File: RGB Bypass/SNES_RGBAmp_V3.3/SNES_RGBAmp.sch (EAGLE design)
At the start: 25 parts

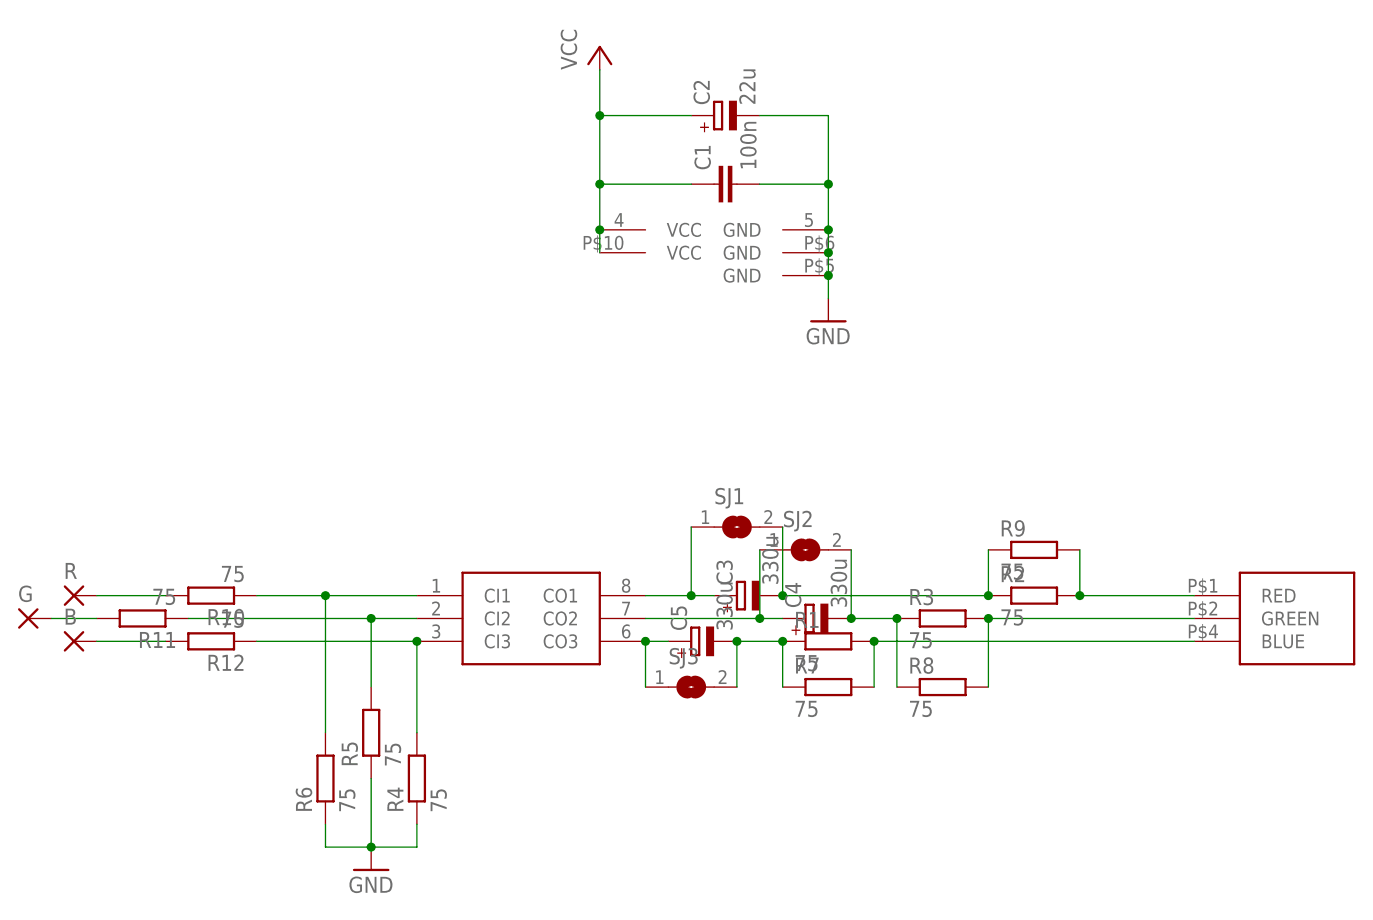
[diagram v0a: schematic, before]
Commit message: RGB Bypass Version Update: - adjustment of wires - mirrored positioning of R, G and B pad - exact values for resistors - add a version with CSYNC-buffering (for 1Chip03 boards and later) - more detailed notes in README
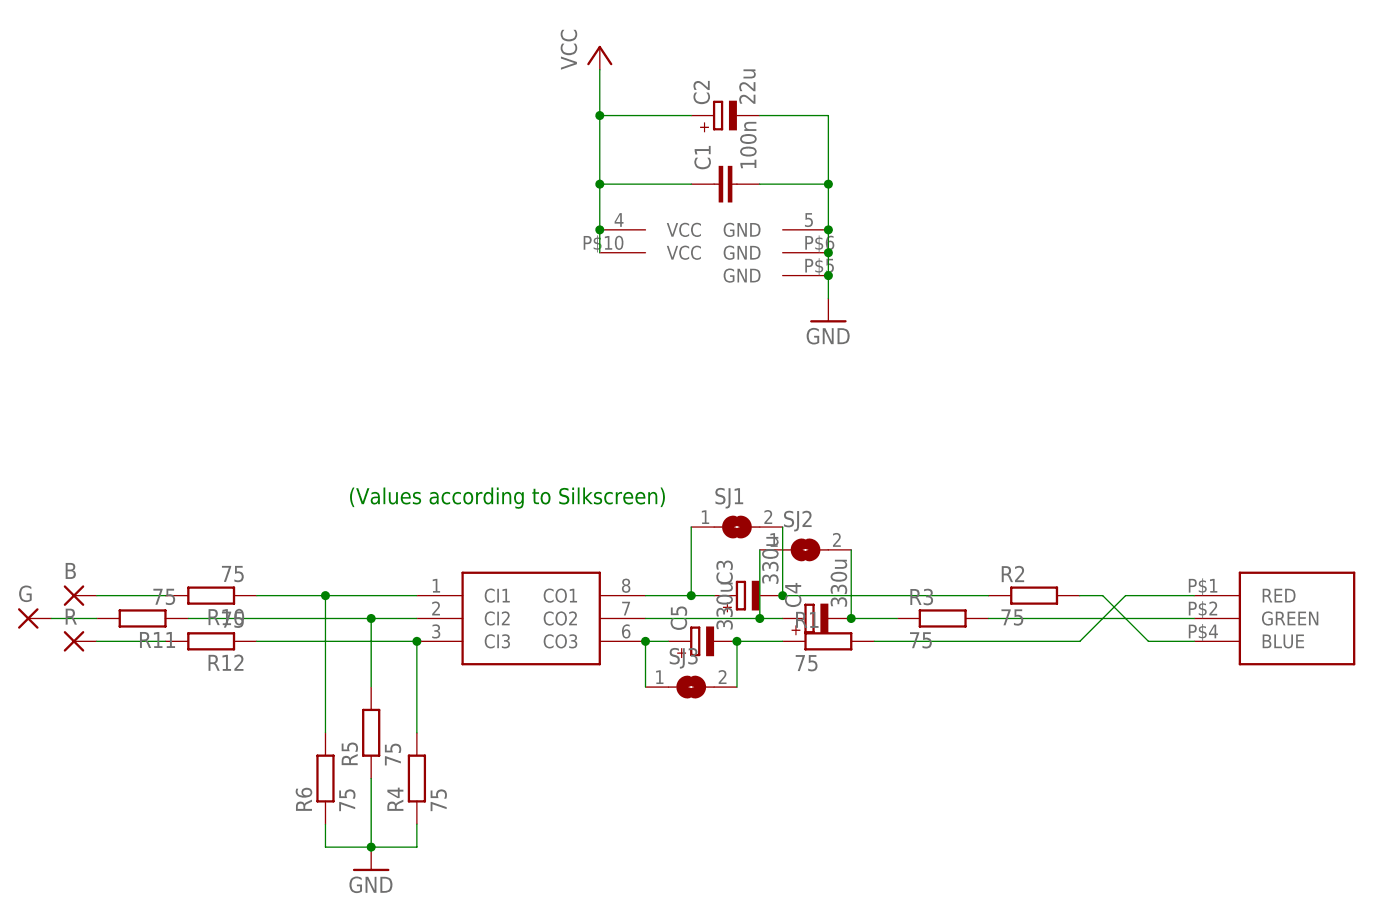
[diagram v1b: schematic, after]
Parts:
- removed R7, R8, R9: 75, snescart:R0805
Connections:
- net N$13: no longer R8.1
- net N$14: now also B.P; no longer R.P
- net N$16: now also R.P; no longer B.P
- net N$4: no longer R9.1
- net N$5: now also U$2G$3.BLUE; no longer R9.2, U$2G$3.RED
- net N$6: no longer R8.2
- net N$8: no longer R7.1
- net N$9: now also U$2G$3.RED; no longer R7.2, U$2G$3.BLUE
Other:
- note added: "(Values according to Silkscreen)"
- moved on the sheet: B, R
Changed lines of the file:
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@@
 <part name="GND1" library="supply1" deviceset="GND" device=""/>
 <part name="C1" library="snescart" deviceset="C0805" device="" value="100n"/>
+<part name="B" library="wirepad" deviceset="SMD2" device=""/>
+<part name="G" library="wirepad" deviceset="SMD2" device=""/>
 <part name="R" library="wirepad" deviceset="SMD2" device=""/>
-<part name="G" library="wirepad" deviceset="SMD2" device=""/>
-<part name="B" library="wirepad" deviceset="SMD2" device=""/>
 <part name="C2" library="rcl" deviceset="CPOL-EU" device="SMCC" value="22u"/>
 <part name="R4" library="snescart" deviceset="R0805" device="" value="75"/>
@@
 <part name="C4" library="rcl" deviceset="CPOL-EU" device="SMCD" value="330u"/>
 <part name="C5" library="rcl" deviceset="CPOL-EU" device="SMCD" value="330u"/>
-<part name="R7" library="snescart" deviceset="R0805" device="" value="75"/>
-<part name="R8" library="snescart" deviceset="R0805" device="" value="75"/>
-<part name="R9" library="snescart" deviceset="R0805" device="" value="75"/>
 <part name="R10" library="snescart" deviceset="R0805" device="" value="75"/>
 <part name="R11" library="snescart" deviceset="R0805" device="" value="75"/>
@@
 <sheet>
 <plain>
+<text x="-20.32" y="10.16" size="1.778" layer="91">(Values according to Silkscreen)</text>
 </plain>
 <instances>
@@
 <instance part="GND1" gate="1" x="33.02" y="30.48"/>
 <instance part="C1" gate="G$1" x="20.32" y="45.72" rot="R90"/>
-<instance part="R" gate="1" x="-50.8" y="0"/>
+<instance part="B" gate="1" x="-50.8" y="0"/>
 <instance part="G" gate="1" x="-55.88" y="-2.54"/>
-<instance part="B" gate="1" x="-50.8" y="-5.08"/>
+<instance part="R" gate="1" x="-50.8" y="-5.08"/>
 <instance part="C2" gate="G$1" x="20.32" y="53.34" rot="R90"/>
 <instance part="R4" gate="G$1" x="-12.7" y="-20.32" rot="R90"/>
@@
 <instance part="C4" gate="G$1" x="30.48" y="-2.54" rot="R90"/>
 <instance part="C5" gate="G$1" x="17.78" y="-5.08" rot="R90"/>
-<instance part="R7" gate="G$1" x="33.02" y="-10.16"/>
-<instance part="R8" gate="G$1" x="45.72" y="-10.16"/>
-<instance part="R9" gate="G$1" x="55.88" y="5.08"/>
 <instance part="R10" gate="G$1" x="-35.56" y="0" rot="R180"/>
 <instance part="R11" gate="G$1" x="-43.18" y="-2.54" rot="R180"/>
@@
 <pinref part="C3" gate="G$1" pin="-"/>
 <wire x1="27.94" y1="0" x2="50.8" y2="0" width="0.1524" layer="91"/>
-<pinref part="R9" gate="G$1" pin="1"/>
-<wire x1="50.8" y1="0" x2="50.8" y2="5.08" width="0.1524" layer="91"/>
-<junction x="50.8" y="0"/>
 <pinref part="SJ1" gate="1" pin="2"/>
 <wire x1="27.94" y1="7.62" x2="27.94" y2="0" width="0.1524" layer="91"/>
@@
 <pinref part="R3" gate="G$1" pin="2"/>
 <wire x1="73.66" y1="-2.54" x2="50.8" y2="-2.54" width="0.1524" layer="91"/>
-<pinref part="R8" gate="G$1" pin="2"/>
-<wire x1="50.8" y1="-10.16" x2="50.8" y2="-2.54" width="0.1524" layer="91"/>
-<junction x="50.8" y="-2.54"/>
 <pinref part="U$2" gate="G$3" pin="GREEN"/>
 </segment>
@@
 <pinref part="C5" gate="G$1" pin="-"/>
 <wire x1="22.86" y1="-5.08" x2="27.94" y2="-5.08" width="0.1524" layer="91"/>
-<pinref part="R7" gate="G$1" pin="1"/>
-<wire x1="27.94" y1="-10.16" x2="27.94" y2="-5.08" width="0.1524" layer="91"/>
-<junction x="27.94" y="-5.08"/>
 <pinref part="SJ3" gate="1" pin="2"/>
 <wire x1="22.86" y1="-10.16" x2="22.86" y2="-5.08" width="0.1524" layer="91"/>
@@
 <segment>
 <pinref part="R1" gate="G$1" pin="2"/>
-<pinref part="R7" gate="G$1" pin="2"/>
-<wire x1="38.1" y1="-5.08" x2="73.66" y2="-5.08" width="0.1524" layer="91"/>
-<wire x1="38.1" y1="-10.16" x2="38.1" y2="-5.08" width="0.1524" layer="91"/>
-<junction x="38.1" y="-5.08"/>
-<pinref part="U$2" gate="G$3" pin="BLUE"/>
+<wire x1="38.1" y1="-5.08" x2="60.96" y2="-5.08" width="0.1524" layer="91"/>
+<wire x1="60.96" y1="-5.08" x2="66.04" y2="0" width="0.1524" layer="91"/>
+<pinref part="U$2" gate="G$3" pin="RED"/>
+<wire x1="66.04" y1="0" x2="73.66" y2="0" width="0.1524" layer="91"/>
 </segment>
 </net>
@@
 <segment>
 <pinref part="R2" gate="G$1" pin="2"/>
-<wire x1="73.66" y1="0" x2="60.96" y2="0" width="0.1524" layer="91"/>
-<pinref part="R9" gate="G$1" pin="2"/>
-<wire x1="60.96" y1="5.08" x2="60.96" y2="0" width="0.1524" layer="91"/>
-<junction x="60.96" y="0"/>
-<pinref part="U$2" gate="G$3" pin="RED"/>
+<wire x1="60.96" y1="0" x2="63.5" y2="0" width="0.1524" layer="91"/>
+<wire x1="63.5" y1="0" x2="68.58" y2="-5.08" width="0.1524" layer="91"/>
+<pinref part="U$2" gate="G$3" pin="BLUE"/>
+<wire x1="68.58" y1="-5.08" x2="73.66" y2="-5.08" width="0.1524" layer="91"/>
 </segment>
 </net>
@@
 <wire x1="40.64" y1="-2.54" x2="35.56" y2="-2.54" width="0.1524" layer="91"/>
 <pinref part="C4" gate="G$1" pin="-"/>
-<pinref part="R8" gate="G$1" pin="1"/>
-<wire x1="40.64" y1="-10.16" x2="40.64" y2="-2.54" width="0.1524" layer="91"/>
-<junction x="40.64" y="-2.54"/>
 <pinref part="SJ2" gate="1" pin="2"/>
 <wire x1="35.56" y1="5.08" x2="35.56" y2="-2.54" width="0.1524" layer="91"/>
@@
 <net name="N$14" class="0">
 <segment>
-<pinref part="R" gate="1" pin="P"/>
+<pinref part="B" gate="1" pin="P"/>
 <wire x1="-48.26" y1="0" x2="-40.64" y2="0" width="0.1524" layer="91"/>
 <pinref part="R10" gate="G$1" pin="2"/>
@@
 <net name="N$16" class="0">
 <segment>
-<pinref part="B" gate="1" pin="P"/>
+<pinref part="R" gate="1" pin="P"/>
 <wire x1="-48.26" y1="-5.08" x2="-40.64" y2="-5.08" width="0.1524" layer="91"/>
 <pinref part="R12" gate="G$1" pin="2"/>

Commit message: Update silkscreen
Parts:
- removed R10, R11, R12: 75, snescart:R0805
- added R7: 9.53k, snescart:R0805
- added R8, R9: 8.45k, snescart:R0805
- R4: value 75 -> 806
- R5, R6: value 75 -> 1.3k
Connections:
- net GND: now also R7.1, R8.1, R9.1; no longer R4.1, R5.1, R6.1
- net N$1: now also R6.1, R9.2; no longer R10.1, R6.2
- net N$13: now also R2.1; no longer R3.1
- net N$14: now also R6.2; no longer R10.2
- net N$15: now also R5.2; no longer R11.2
- net N$16: now also R4.2; no longer R12.2
- net N$2: now also R5.1, R8.2; no longer R11.1, R5.2
- net N$3: now also R4.1, R7.2; no longer R12.1, R4.2
- net N$4: now also R3.1; no longer R2.1
- net N$5: now also R3.2; no longer R2.2
- net N$6: now also R2.2; no longer R3.2
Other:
- moved on the sheet: R2, R3, R4, R5, R6
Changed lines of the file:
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@@
 <?xml version="1.0" encoding="utf-8"?>
 <!DOCTYPE eagle SYSTEM "eagle.dtd">
-<eagle version="6.4">
+<eagle version="7.5.0">
 <drawing>
 <settings>
@@
 <parts>
 <part name="U$1" library="snescart" deviceset="THS7314" device=""/>
+<part name="R3" library="snescart" deviceset="R0805" device="" value="75"/>
 <part name="R2" library="snescart" deviceset="R0805" device="" value="75"/>
-<part name="R3" library="snescart" deviceset="R0805" device="" value="75"/>
 <part name="R1" library="snescart" deviceset="R0805" device="" value="75"/>
 <part name="P+1" library="supply1" deviceset="VCC" device=""/>
@@
 <part name="R" library="wirepad" deviceset="SMD2" device=""/>
 <part name="C2" library="rcl" deviceset="CPOL-EU" device="SMCC" value="22u"/>
-<part name="R4" library="snescart" deviceset="R0805" device="" value="75"/>
-<part name="R5" library="snescart" deviceset="R0805" device="" value="75"/>
-<part name="R6" library="snescart" deviceset="R0805" device="" value="75"/>
+<part name="R7" library="snescart" deviceset="R0805" device="" value="9.53k"/>
+<part name="R8" library="snescart" deviceset="R0805" device="" value="8.45k"/>
+<part name="R9" library="snescart" deviceset="R0805" device="" value="8.45k"/>
 <part name="GND2" library="supply1" deviceset="GND" device=""/>
 <part name="C3" library="rcl" deviceset="CPOL-EU" device="SMCD" value="330u"/>
 <part name="C4" library="rcl" deviceset="CPOL-EU" device="SMCD" value="330u"/>
 <part name="C5" library="rcl" deviceset="CPOL-EU" device="SMCD" value="330u"/>
-<part name="R10" library="snescart" deviceset="R0805" device="" value="75"/>
-<part name="R11" library="snescart" deviceset="R0805" device="" value="75"/>
-<part name="R12" library="snescart" deviceset="R0805" device="" value="75"/>
+<part name="R6" library="snescart" deviceset="R0805" device="" value="1.3k"/>
+<part name="R5" library="snescart" deviceset="R0805" device="" value="1.3k"/>
+<part name="R4" library="snescart" deviceset="R0805" device="" value="806"/>
 <part name="SJ1" library="jumper" deviceset="SJ" device=""/>
 <part name="SJ2" library="jumper" deviceset="SJ" device=""/>
@@
 <instances>
 <instance part="U$1" gate="G$1" x="0" y="-2.54"/>
-<instance part="R2" gate="G$1" x="55.88" y="0"/>
-<instance part="R3" gate="G$1" x="45.72" y="-2.54"/>
+<instance part="R3" gate="G$1" x="55.88" y="0"/>
+<instance part="R2" gate="G$1" x="45.72" y="-2.54"/>
 <instance part="R1" gate="G$1" x="33.02" y="-5.08"/>
 <instance part="U$1" gate="G$2" x="20.32" y="40.64" rot="R90"/>
@@
 <instance part="R" gate="1" x="-50.8" y="-5.08"/>
 <instance part="C2" gate="G$1" x="20.32" y="53.34" rot="R90"/>
-<instance part="R4" gate="G$1" x="-12.7" y="-20.32" rot="R90"/>
-<instance part="R5" gate="G$1" x="-17.78" y="-15.24" rot="R90"/>
-<instance part="R6" gate="G$1" x="-22.86" y="-20.32" rot="R90"/>
+<instance part="R7" gate="G$1" x="-12.7" y="-20.32" rot="R90"/>
+<instance part="R8" gate="G$1" x="-17.78" y="-15.24" rot="R90"/>
+<instance part="R9" gate="G$1" x="-22.86" y="-20.32" rot="R90"/>
 <instance part="GND2" gate="1" x="-17.78" y="-30.48"/>
 <instance part="C3" gate="G$1" x="22.86" y="0" rot="R90"/>
 <instance part="C4" gate="G$1" x="30.48" y="-2.54" rot="R90"/>
 <instance part="C5" gate="G$1" x="17.78" y="-5.08" rot="R90"/>
-<instance part="R10" gate="G$1" x="-35.56" y="0" rot="R180"/>
-<instance part="R11" gate="G$1" x="-43.18" y="-2.54" rot="R180"/>
-<instance part="R12" gate="G$1" x="-35.56" y="-5.08" rot="R180"/>
+<instance part="R6" gate="G$1" x="-35.56" y="0" rot="R180"/>
+<instance part="R5" gate="G$1" x="-43.18" y="-2.54" rot="R180"/>
+<instance part="R4" gate="G$1" x="-35.56" y="-5.08" rot="R180"/>
 <instance part="SJ1" gate="1" x="22.86" y="7.62"/>
 <instance part="SJ2" gate="1" x="30.48" y="5.08"/>
@@
 <segment>
 <pinref part="U$1" gate="G$1" pin="CI1"/>
-<pinref part="R6" gate="G$1" pin="2"/>
+<pinref part="R9" gate="G$1" pin="2"/>
 <wire x1="-30.48" y1="0" x2="-22.86" y2="0" width="0.1524" layer="91"/>
 <wire x1="-22.86" y1="0" x2="-12.7" y2="0" width="0.1524" layer="91"/>
 <wire x1="-22.86" y1="-15.24" x2="-22.86" y2="0" width="0.1524" layer="91"/>
 <junction x="-22.86" y="0"/>
-<pinref part="R10" gate="G$1" pin="1"/>
+<pinref part="R6" gate="G$1" pin="1"/>
 </segment>
 </net>
@@
 <pinref part="U$1" gate="G$1" pin="CI2"/>
 <wire x1="-12.7" y1="-2.54" x2="-17.78" y2="-2.54" width="0.1524" layer="91"/>
-<pinref part="R5" gate="G$1" pin="2"/>
+<pinref part="R8" gate="G$1" pin="2"/>
 <wire x1="-17.78" y1="-2.54" x2="-38.1" y2="-2.54" width="0.1524" layer="91"/>
 <wire x1="-17.78" y1="-10.16" x2="-17.78" y2="-2.54" width="0.1524" layer="91"/>
 <junction x="-17.78" y="-2.54"/>
-<pinref part="R11" gate="G$1" pin="1"/>
+<pinref part="R5" gate="G$1" pin="1"/>
 </segment>
 </net>
@@
 <segment>
 <pinref part="U$1" gate="G$1" pin="CI3"/>
-<pinref part="R4" gate="G$1" pin="2"/>
+<pinref part="R7" gate="G$1" pin="2"/>
 <wire x1="-30.48" y1="-5.08" x2="-12.7" y2="-5.08" width="0.1524" layer="91"/>
 <wire x1="-12.7" y1="-15.24" x2="-12.7" y2="-5.08" width="0.1524" layer="91"/>
 <junction x="-12.7" y="-5.08"/>
-<pinref part="R12" gate="G$1" pin="1"/>
+<pinref part="R4" gate="G$1" pin="1"/>
 </segment>
 </net>
 <net name="N$4" class="0">
 <segment>
-<pinref part="R2" gate="G$1" pin="1"/>
+<pinref part="R3" gate="G$1" pin="1"/>
 <pinref part="C3" gate="G$1" pin="-"/>
 <wire x1="27.94" y1="0" x2="50.8" y2="0" width="0.1524" layer="91"/>
@@
 <net name="N$6" class="0">
 <segment>
-<pinref part="R3" gate="G$1" pin="2"/>
+<pinref part="R2" gate="G$1" pin="2"/>
 <wire x1="73.66" y1="-2.54" x2="50.8" y2="-2.54" width="0.1524" layer="91"/>
 <pinref part="U$2" gate="G$3" pin="GREEN"/>
@@
 </segment>
 <segment>
-<pinref part="R5" gate="G$1" pin="1"/>
+<pinref part="R8" gate="G$1" pin="1"/>
 <pinref part="GND2" gate="1" pin="GND"/>
 <wire x1="-17.78" y1="-20.32" x2="-17.78" y2="-27.94" width="0.1524" layer="91"/>
-<pinref part="R6" gate="G$1" pin="1"/>
+<pinref part="R9" gate="G$1" pin="1"/>
 <wire x1="-17.78" y1="-27.94" x2="-22.86" y2="-27.94" width="0.1524" layer="91"/>
 <wire x1="-22.86" y1="-27.94" x2="-22.86" y2="-25.4" width="0.1524" layer="91"/>
 <junction x="-17.78" y="-27.94"/>
-<pinref part="R4" gate="G$1" pin="1"/>
+<pinref part="R7" gate="G$1" pin="1"/>
 <wire x1="-12.7" y1="-25.4" x2="-12.7" y2="-27.94" width="0.1524" layer="91"/>
 <wire x1="-12.7" y1="-27.94" x2="-17.78" y2="-27.94" width="0.1524" layer="91"/>
@@
 <net name="N$5" class="0">
 <segment>
-<pinref part="R2" gate="G$1" pin="2"/>
+<pinref part="R3" gate="G$1" pin="2"/>
 <wire x1="60.96" y1="0" x2="63.5" y2="0" width="0.1524" layer="91"/>
 <wire x1="63.5" y1="0" x2="68.58" y2="-5.08" width="0.1524" layer="91"/>
@@
 <net name="N$13" class="0">
 <segment>
-<pinref part="R3" gate="G$1" pin="1"/>
+<pinref part="R2" gate="G$1" pin="1"/>
 <wire x1="40.64" y1="-2.54" x2="35.56" y2="-2.54" width="0.1524" layer="91"/>
 <pinref part="C4" gate="G$1" pin="-"/>
@@
 <pinref part="B" gate="1" pin="P"/>
 <wire x1="-48.26" y1="0" x2="-40.64" y2="0" width="0.1524" layer="91"/>
-<pinref part="R10" gate="G$1" pin="2"/>
+<pinref part="R6" gate="G$1" pin="2"/>
 </segment>
 </net>
@@
 <pinref part="G" gate="1" pin="P"/>
 <wire x1="-48.26" y1="-2.54" x2="-53.34" y2="-2.54" width="0.1524" layer="91"/>
-<pinref part="R11" gate="G$1" pin="2"/>
+<pinref part="R5" gate="G$1" pin="2"/>
 </segment>
 </net>
@@
 <pinref part="R" gate="1" pin="P"/>
 <wire x1="-48.26" y1="-5.08" x2="-40.64" y2="-5.08" width="0.1524" layer="91"/>
-<pinref part="R12" gate="G$1" pin="2"/>
-</segment>
-</net>
+<pinref part="R4" gate="G$1" pin="2"/>
+</segment>
+</net>
